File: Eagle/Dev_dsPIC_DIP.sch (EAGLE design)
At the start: 34 parts, among them IC1 DSPIC33FJ64MC802-SP, P1 Vin, P2 5V

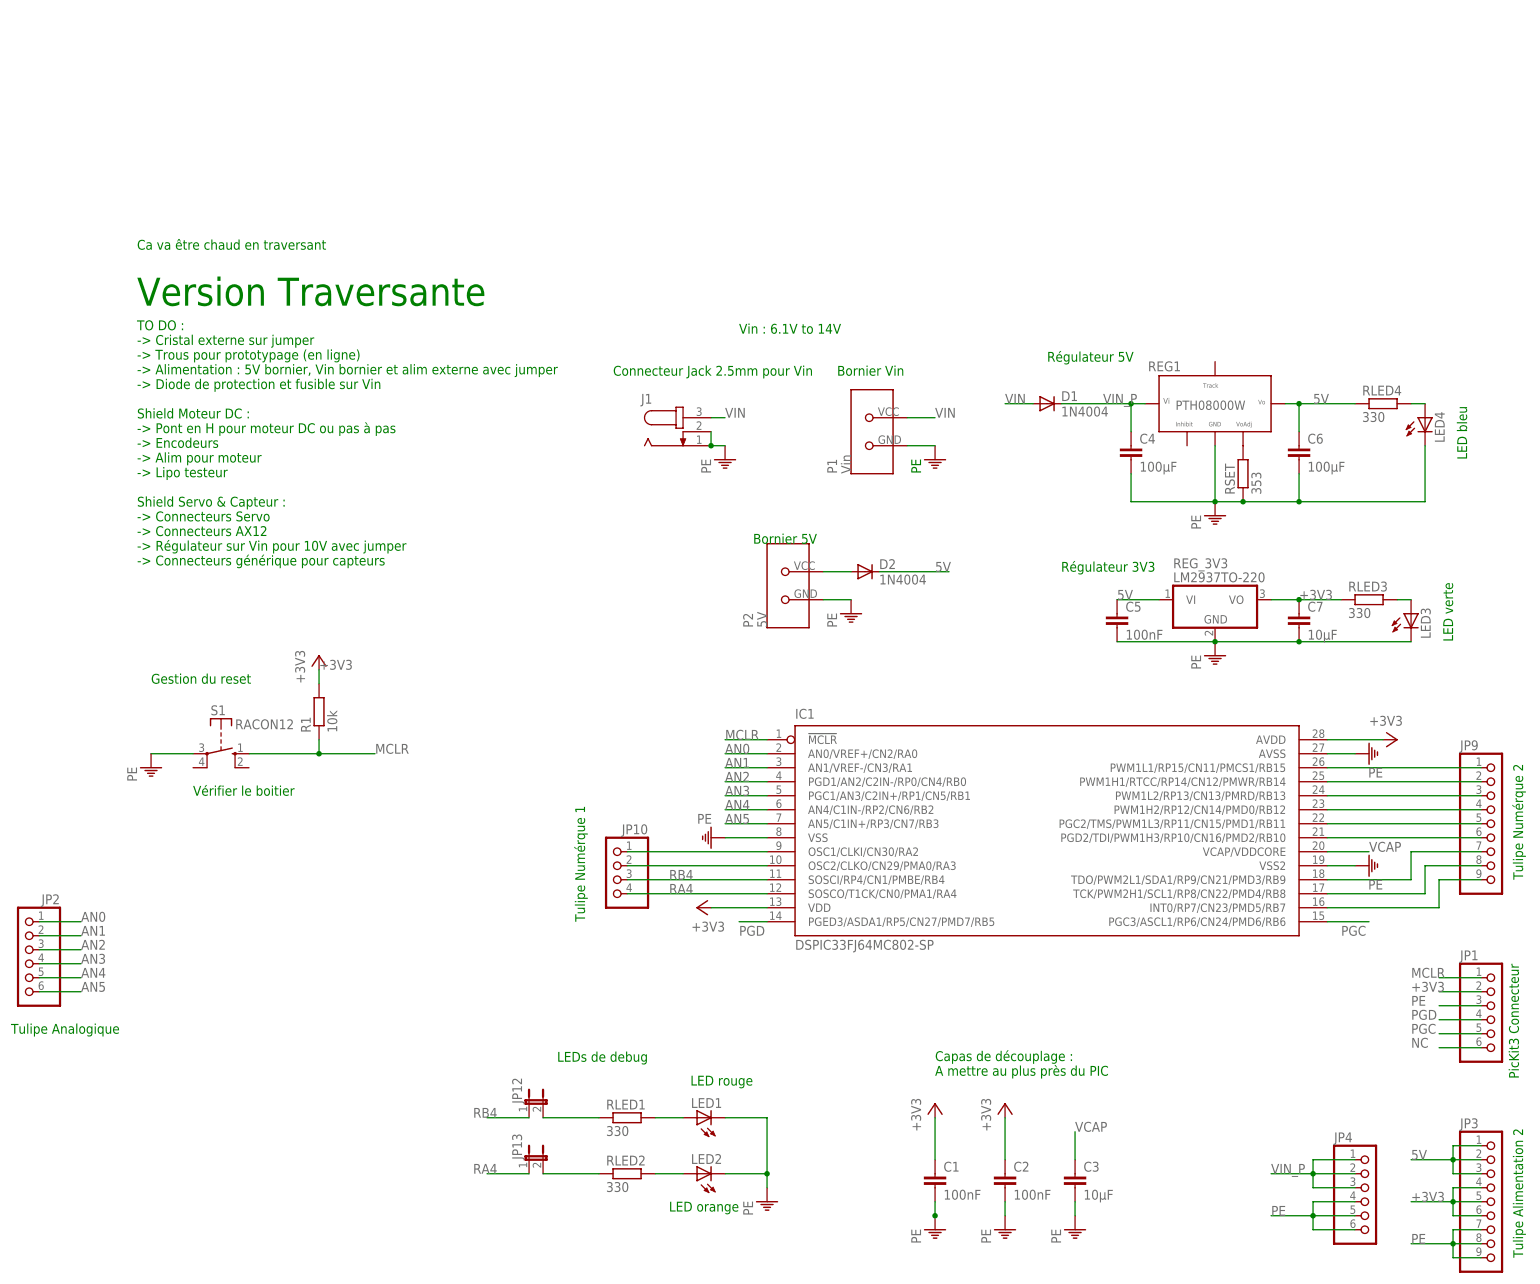
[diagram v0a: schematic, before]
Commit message: Base dsPIC v1.1 & Shield Moteur sans connecteur
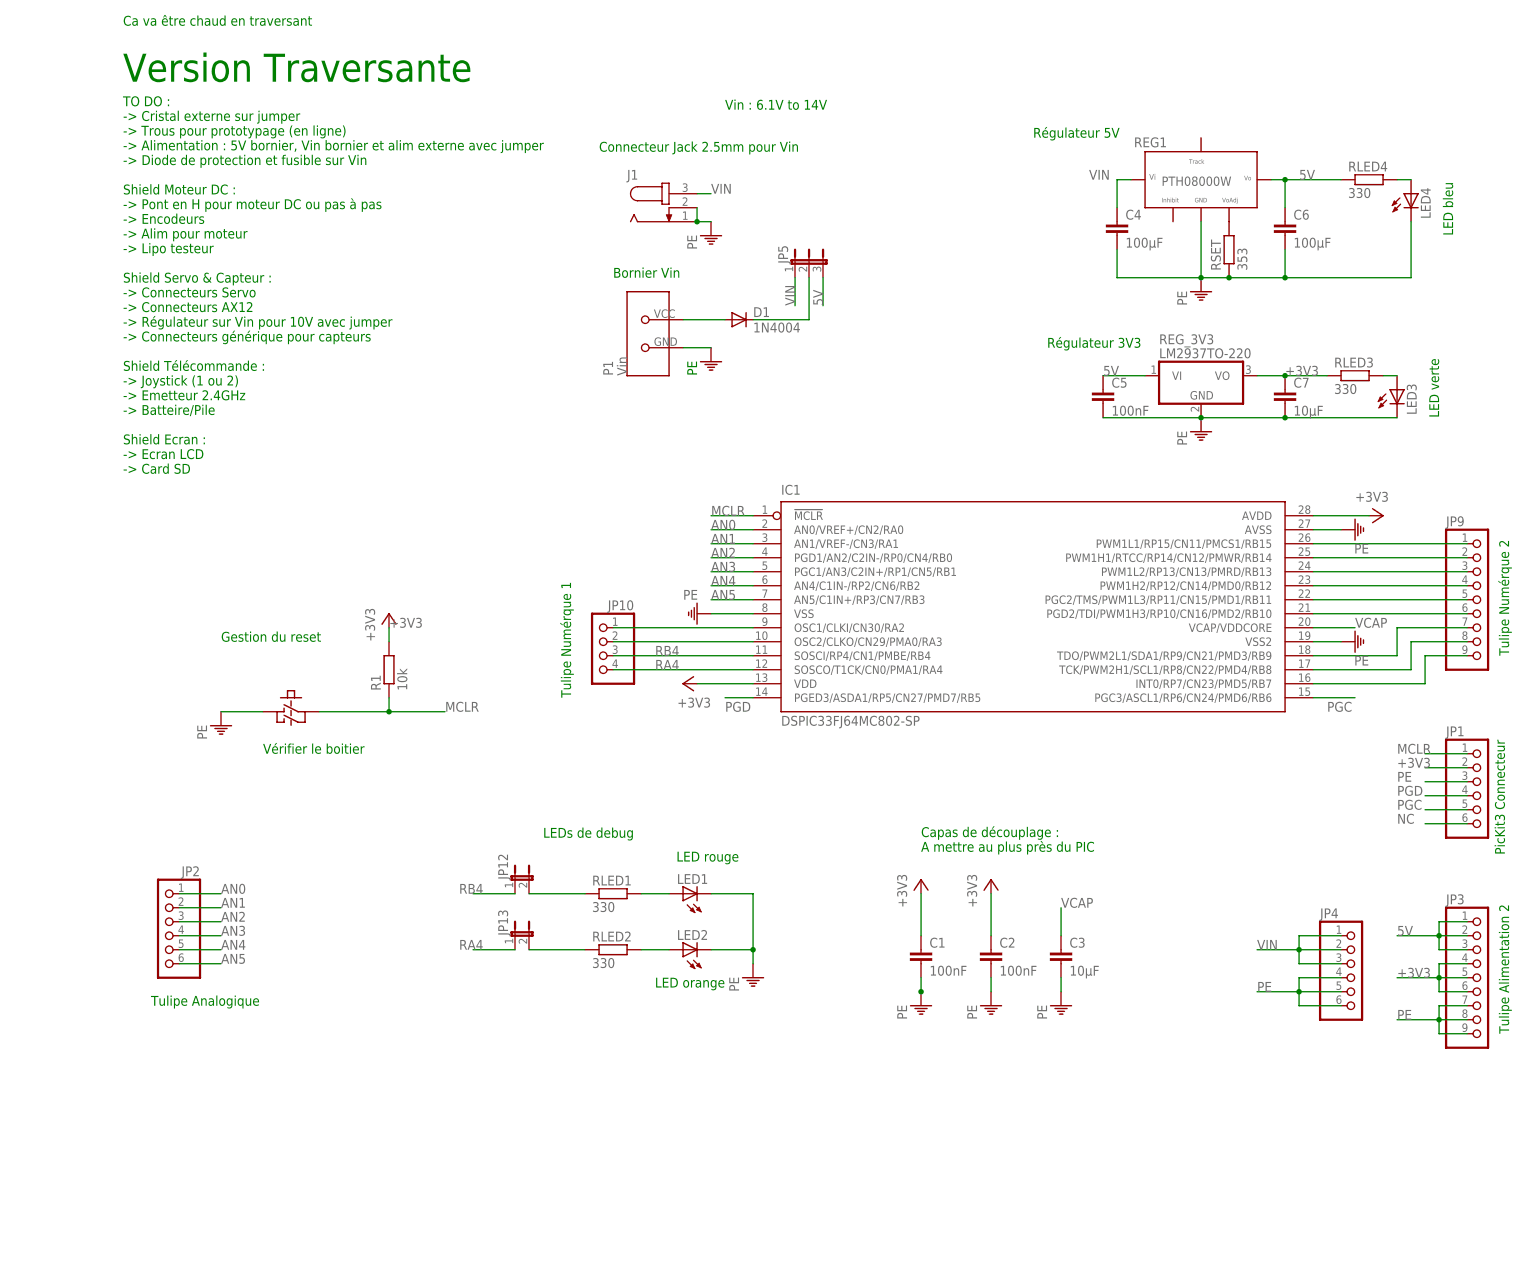
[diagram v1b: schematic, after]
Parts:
- removed D2: 1N4004, diode:1N4004
- removed P2: 5V, Perso:BORNIER_3.5MM
- removed S1: RACON12, switch-misc:RACON12
- added JP5: (no value), jumper:JP2E
- added U$1: BP, Perso:BP
- C3: device rcl:C-EU050-035X075 -> rcl:C-EU025-030X050
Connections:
- removed net VIN_P: C4.1, D1.C, JP4.1, JP4.2, JP4.3, REG1.3
- new net VCC: D1.C, JP5.2
- net 5V: now also JP5.3; no longer D2.C
- net MCLR: now also U$1.3; no longer S1.S
- net N$17: now also D1.A, P1.VCC; no longer D2.A, P2.VCC
- net PE: now also U$1.1; no longer P2.GND, S1.P
- net VIN: now also C4.1, JP4.1, JP4.2, JP4.3, JP5.1, REG1.3; no longer D1.A, P1.VCC
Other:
- note removed: "Bornier 5V"
- moved on the sheet: C1, C2, C3, C4, C5, C6, C7, D1, IC1, J1, JP1, JP10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

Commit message: Petit changement au routage et au template
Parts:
- C1: device rcl:C-EU102-043X133 -> rcl:C-EU050-035X075
- IC1: value DSPIC33FJ64MC802-SP -> DSPIC33FJ128MC802-SP; device microchip-dspic33fjxxmc:DSPIC33FJ64MC802-SP -> microchip-dspic33fjxxmc:DSPIC33FJ128MC802-SP
- R1, RLED1, RLED2, RLED3, RLED4, RSET: device rcl:R-EU_0204/7 -> rcl:R-EU_0207/10
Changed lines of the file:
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@@
 <grid distance="0.1" unitdist="inch" unit="inch" style="lines" multiple="1" display="no" altdistance="0.01" altunitdist="inch" altunit="inch"/>
 <layers>
-<layer number="1" name="Top" color="4" fill="1" visible="no" active="no"/>
-<layer number="2" name="Route2" color="1" fill="3" visible="no" active="no"/>
-<layer number="3" name="Route3" color="4" fill="3" visible="no" active="no"/>
-<layer number="4" name="Route4" color="1" fill="4" visible="no" active="no"/>
-<layer number="5" name="Route5" color="4" fill="4" visible="no" active="no"/>
-<layer number="6" name="Route6" color="1" fill="8" visible="no" active="no"/>
-<layer number="7" name="Route7" color="4" fill="8" visible="no" active="no"/>
-<layer number="8" name="Route8" color="1" fill="2" visible="no" active="no"/>
-<layer number="9" name="Route9" color="4" fill="2" visible="no" active="no"/>
-<layer number="10" name="Route10" color="1" fill="7" visible="no" active="no"/>
-<layer number="11" name="Route11" color="4" fill="7" visible="no" active="no"/>
-<layer number="12" name="Route12" color="1" fill="5" visible="no" active="no"/>
-<layer number="13" name="Route13" color="4" fill="5" visible="no" active="no"/>
-<layer number="14" name="Route14" color="1" fill="6" visible="no" active="no"/>
-<layer number="15" name="Route15" color="4" fill="6" visible="no" active="no"/>
-<layer number="16" name="Bottom" color="1" fill="1" visible="no" active="no"/>
-<layer number="17" name="Pads" color="2" fill="1" visible="no" active="no"/>
-<layer number="18" name="Vias" color="2" fill="1" visible="no" active="no"/>
-<layer number="19" name="Unrouted" color="6" fill="1" visible="no" active="no"/>
-<layer number="20" name="Dimension" color="15" fill="1" visible="no" active="no"/>
-<layer number="21" name="tPlace" color="7" fill="1" visible="no" active="no"/>
-<layer number="22" name="bPlace" color="7" fill="1" visible="no" active="no"/>
-<layer number="23" name="tOrigins" color="15" fill="1" visible="no" active="no"/>
-<layer number="24" name="bOrigins" color="15" fill="1" visible="no" active="no"/>
-<layer number="25" name="tNames" color="7" fill="1" visible="no" active="no"/>
-<layer number="26" name="bNames" color="7" fill="1" visible="no" active="no"/>
-<layer number="27" name="tValues" color="7" fill="1" visible="no" active="no"/>
-<layer number="28" name="bValues" color="7" fill="1" visible="no" active="no"/>
+<layer number="1" name="Top" color="4" fill="1" visible="yes" active="no"/>
+<layer number="2" name="Route2" color="1" fill="3" visible="yes" active="no"/>
+<layer number="3" name="Route3" color="4" fill="3" visible="yes" active="no"/>
+<layer number="4" name="Route4" color="1" fill="4" visible="yes" active="no"/>
+<layer number="5" name="Route5" color="4" fill="4" visible="yes" active="no"/>
+<layer number="6" name="Route6" color="1" fill="8" visible="yes" active="no"/>
+<layer number="7" name="Route7" color="4" fill="8" visible="yes" active="no"/>
+<layer number="8" name="Route8" color="1" fill="2" visible="yes" active="no"/>
+<layer number="9" name="Route9" color="4" fill="2" visible="yes" active="no"/>
+<layer number="10" name="Route10" color="1" fill="7" visible="yes" active="no"/>
+<layer number="11" name="Route11" color="4" fill="7" visible="yes" active="no"/>
+<layer number="12" name="Route12" color="1" fill="5" visible="yes" active="no"/>
+<layer number="13" name="Route13" color="4" fill="5" visible="yes" active="no"/>
+<layer number="14" name="Route14" color="1" fill="6" visible="yes" active="no"/>
+<layer number="15" name="Route15" color="4" fill="6" visible="yes" active="no"/>
+<layer number="16" name="Bottom" color="1" fill="1" visible="yes" active="no"/>
+<layer number="17" name="Pads" color="2" fill="1" visible="yes" active="no"/>
+<layer number="18" name="Vias" color="2" fill="1" visible="yes" active="no"/>
+<layer number="19" name="Unrouted" color="6" fill="1" visible="yes" active="no"/>
+<layer number="20" name="Dimension" color="15" fill="1" visible="yes" active="no"/>
+<layer number="21" name="tPlace" color="7" fill="1" visible="yes" active="no"/>
+<layer number="22" name="bPlace" color="7" fill="1" visible="yes" active="no"/>
+<layer number="23" name="tOrigins" color="15" fill="1" visible="yes" active="no"/>
+<layer number="24" name="bOrigins" color="15" fill="1" visible="yes" active="no"/>
+<layer number="25" name="tNames" color="7" fill="1" visible="yes" active="no"/>
+<layer number="26" name="bNames" color="7" fill="1" visible="yes" active="no"/>
+<layer number="27" name="tValues" color="7" fill="1" visible="yes" active="no"/>
+<layer number="28" name="bValues" color="7" fill="1" visible="yes" active="no"/>
 <layer number="29" name="tStop" color="7" fill="3" visible="no" active="no"/>
 <layer number="30" name="bStop" color="7" fill="6" visible="no" active="no"/>
@@
 <layer number="35" name="tGlue" color="7" fill="4" visible="no" active="no"/>
 <layer number="36" name="bGlue" color="7" fill="5" visible="no" active="no"/>
-<layer number="37" name="tTest" color="7" fill="1" visible="no" active="no"/>
-<layer number="38" name="bTest" color="7" fill="1" visible="no" active="no"/>
+<layer number="37" name="tTest" color="7" fill="1" visible="yes" active="no"/>
+<layer number="38" name="bTest" color="7" fill="1" visible="yes" active="no"/>
 <layer number="39" name="tKeepout" color="4" fill="11" visible="no" active="no"/>
 <layer number="40" name="bKeepout" color="1" fill="11" visible="no" active="no"/>
@@
 <layer number="44" name="Drills" color="7" fill="1" visible="no" active="no"/>
 <layer number="45" name="Holes" color="7" fill="1" visible="no" active="no"/>
-<layer number="46" name="Milling" color="3" fill="1" visible="no" active="no"/>
-<layer number="47" name="Measures" color="7" fill="1" visible="no" active="no"/>
-<layer number="48" name="Document" color="7" fill="1" visible="no" active="no"/>
-<layer number="49" name="Reference" color="7" fill="1" visible="no" active="no"/>
-<layer number="50" name="dxf" color="7" fill="1" visible="no" active="no"/>
-<layer number="51" name="tDocu" color="7" fill="1" visible="no" active="no"/>
-<layer number="52" name="bDocu" color="7" fill="1" visible="no" active="no"/>
+<layer number="46" name="Milling" color="3" fill="1" visible="yes" active="no"/>
+<layer number="47" name="Measures" color="7" fill="1" visible="yes" active="no"/>
+<layer number="48" name="Document" color="7" fill="1" visible="yes" active="no"/>
+<layer number="49" name="Reference" color="7" fill="1" visible="yes" active="no"/>
+<layer number="50" name="dxf" color="7" fill="1" visible="yes" active="no"/>
+<layer number="51" name="tDocu" color="7" fill="1" visible="yes" active="no"/>
+<layer number="52" name="bDocu" color="7" fill="1" visible="yes" active="no"/>
 <layer number="91" name="Nets" color="2" fill="1" visible="yes" active="yes"/>
 <layer number="92" name="Busses" color="1" fill="1" visible="yes" active="yes"/>
@@
 </classes>
 <parts>
-<part name="IC1" library="microchip-dspic33fjxxmc" deviceset="DSPIC33FJ64MC802" device="-SP"/>
-<part name="C1" library="rcl" deviceset="C-EU" device="102-043X133" value="100nF"/>
+<part name="IC1" library="microchip-dspic33fjxxmc" deviceset="DSPIC33FJ128MC802" device="-SP"/>
+<part name="C1" library="rcl" deviceset="C-EU" device="050-035X075" value="100nF"/>
 <part name="C2" library="rcl" deviceset="C-EU" device="050-035X075" value="100nF"/>
 <part name="C3" library="rcl" deviceset="C-EU" device="025-030X050" value="10µF"/>
-<part name="R1" library="rcl" deviceset="R-EU_" device="0204/7" value="10k"/>
+<part name="R1" library="rcl" deviceset="R-EU_" device="0207/10" value="10k"/>
 <part name="+3V1" library="supply1" deviceset="+3V3" device=""/>
 <part name="+3V2" library="supply1" deviceset="+3V3" device=""/>
@@
 <part name="JP9" library="pinhead" deviceset="PINHD-1X9" device=""/>
 <part name="JP10" library="pinhead" deviceset="PINHD-1X4" device=""/>
-<part name="RLED1" library="rcl" deviceset="R-EU_" device="0204/7" value="330"/>
-<part name="RLED2" library="rcl" deviceset="R-EU_" device="0204/7" value="330"/>
+<part name="RLED1" library="rcl" deviceset="R-EU_" device="0207/10" value="330"/>
+<part name="RLED2" library="rcl" deviceset="R-EU_" device="0207/10" value="330"/>
 <part name="LED1" library="led" deviceset="LED" device="3MM"/>
 <part name="LED2" library="led" deviceset="LED" device="3MM"/>
 <part name="PE8" library="supply1" deviceset="PE" device=""/>
-<part name="RLED3" library="rcl" deviceset="R-EU_" device="0204/7" value="330"/>
+<part name="RLED3" library="rcl" deviceset="R-EU_" device="0207/10" value="330"/>
 <part name="LED3" library="led" deviceset="LED" device="3MM"/>
 <part name="JP12" library="jumper" deviceset="JP1E" device=""/>
@@
 <part name="GND7" library="supply1" deviceset="PE" device=""/>
 <part name="REG1" library="Perso" deviceset="PTH08000W(EUS)" device=""/>
-<part name="RSET" library="rcl" deviceset="R-EU_" device="0204/7" value="353"/>
+<part name="RSET" library="rcl" deviceset="R-EU_" device="0207/10" value="353"/>
 <part name="C4" library="rcl" deviceset="C-EU" device="050-035X075" value="100µF"/>
 <part name="C6" library="rcl" deviceset="C-EU" device="050-035X075" value="100µF"/>
-<part name="RLED4" library="rcl" deviceset="R-EU_" device="0204/7" value="330"/>
+<part name="RLED4" library="rcl" deviceset="R-EU_" device="0207/10" value="330"/>
 <part name="LED4" library="led" deviceset="LED" device="3MM"/>
 <part name="GND5" library="supply1" deviceset="PE" device=""/>

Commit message: Carte de DEV base presque finit
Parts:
- C3: device rcl:C-EU025-030X050 -> rcl:CPOL-EUE2.5-5V
- C4, C6: device rcl:C-EU050-035X075 -> rcl:CPOL-EUE3.5-8
- R1, RLED1, RLED2, RLED3, RLED4, RSET: device rcl:R-EU_0207/10 -> Perso:RES_PERSO
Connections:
- net 5V: now also C6.+; no longer C6.1
- net PE: now also C3.-, C4.-, C6.-; no longer C3.2, C4.2, C6.2
- net VCAP: now also C3.+; no longer C3.1
- net VIN: now also C4.+; no longer C4.1
